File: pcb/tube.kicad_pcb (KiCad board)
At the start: 2 copper layers, 99.1 x 116.8 mm, 80 parts, among them J1 Screw_Terminal_01x02, J10 LED_[5..8], J11 LED_[1..4], J2 Screw_Terminal_01x02, J3 Screw_Terminal_01x02, J4 Conn_01x04_Pin, J5 Conn_01x08_Pin, J6 Conn_01x05_Pin, U1 INA226, U10 74LS32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

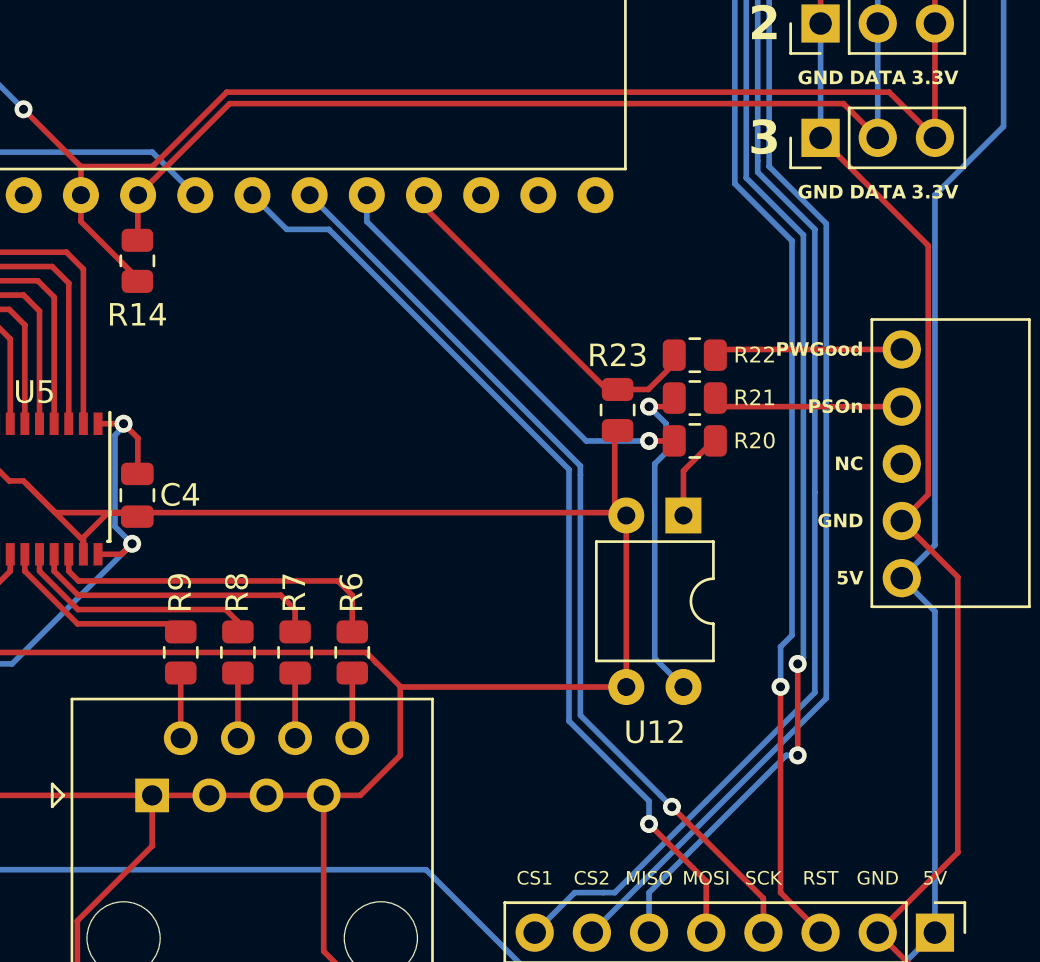
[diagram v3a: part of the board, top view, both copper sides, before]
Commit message: PCB: Add Optocoppler For PWGood
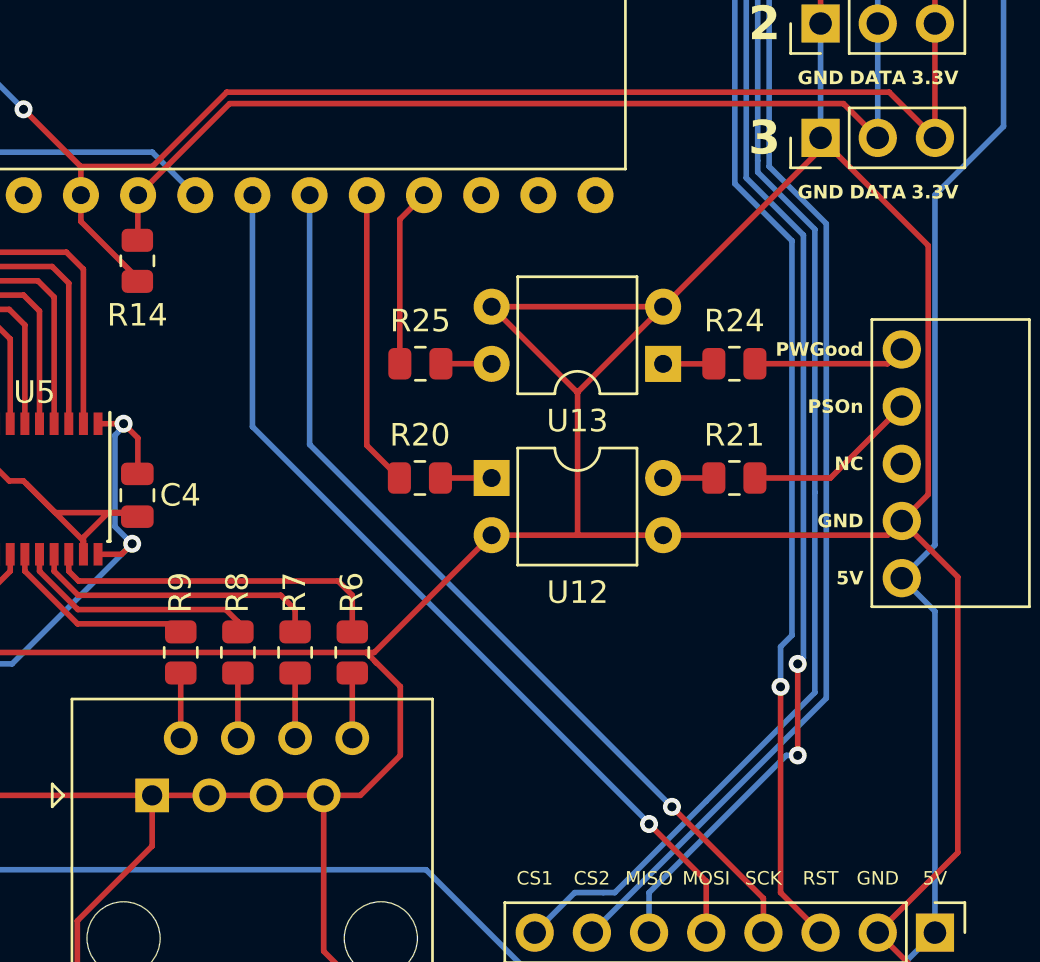
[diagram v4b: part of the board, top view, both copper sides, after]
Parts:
- removed R22: 5kΩ, Resistor_SMD:R_0805_2012Metric
- removed R23: 10kΩ, Resistor_SMD:R_0805_2012Metric
- added R24: 330Ω, Resistor_SMD:R_0805_2012Metric, F.Cu at (227.3, 184.8)
- added R25: 330Ω, Resistor_SMD:R_0805_2012Metric, F.Cu at (213.4, 184.8)
- added U13: PC817, Package_DIP:DIP-4_W7.62mm, F.Cu at (224.1, 184.8)
- moved R20 12.3 mm to (213.3, 189.9)
- moved U12 8.69 mm to (216.5, 189.9), turned to 0 degrees
- moved R21 3.96 mm to (227.3, 189.9)
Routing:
- net GND: track 1026.6 -> 1044.9 mm
- net Net-(R21-Pad2): track 14.7 -> 2.25 mm, vias 1 -> 0
- net Net-(U4-29_TX7): track 16.1 -> 8.45 mm
- net Net-(U4-28_RX7): track 19.0 -> 13.2 mm, vias 1 -> 0
- net Net-(R25-Pad2): track 0.00 -> 2.25 mm
- net Net-(R24-Pad1): track 0.00 -> 2.25 mm
- net Net-(R20-Pad1): track 3.86 -> 2.26 mm
- net /PWGood: track 8.37 -> 6.79 mm
- net /MOSI: track 42.2 -> 41.1 mm
- net /PSOn: track 8.64 -> 8.04 mm

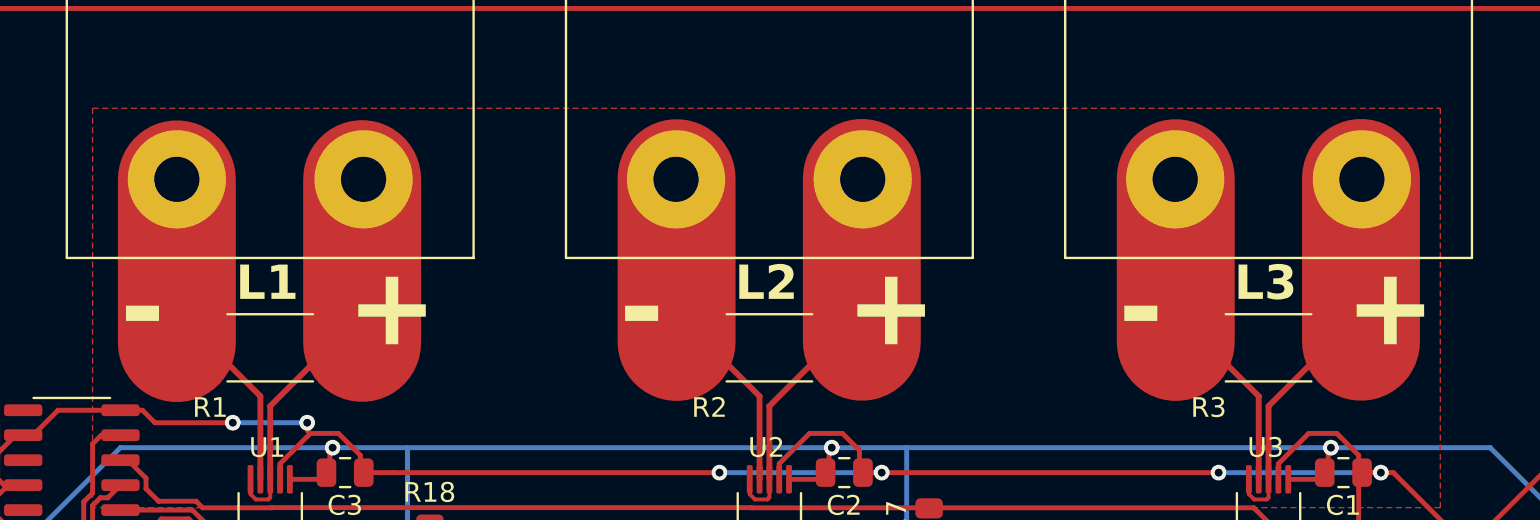
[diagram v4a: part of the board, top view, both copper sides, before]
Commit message: PCB: Tweak Shunt Trace
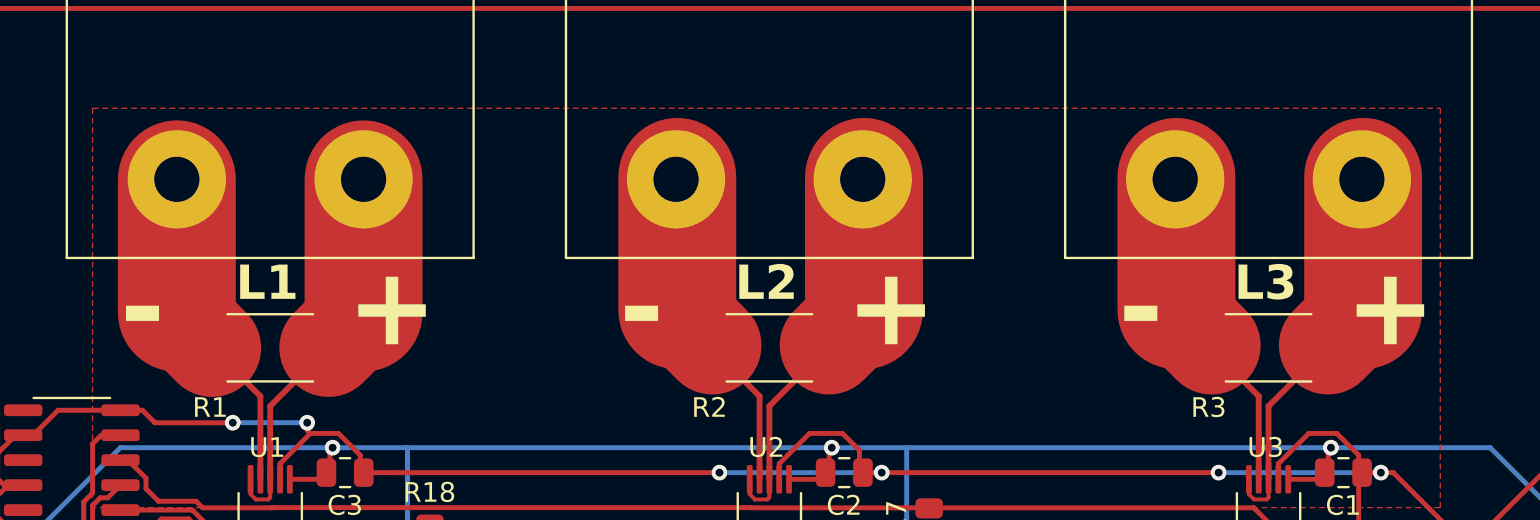
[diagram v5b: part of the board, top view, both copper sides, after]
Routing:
- net /Vin3+: track 19.1 -> 20.1 mm
- net /Vin1-: track 16.0 -> 17.0 mm
- net /Vin1+: track 19.1 -> 20.1 mm
- net /Vin3-: track 16.0 -> 17.0 mm
- net /Vin2-: track 16.0 -> 17.0 mm
- net /Vin2+: track 19.1 -> 20.1 mm
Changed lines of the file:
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@@
   (segment (start 172.235 131.57) (end 176.045 131.57) (width 0.25) (layer "B.Cu") (net 2))
   (segment (start 231.29 143) (end 230.02 144.27) (width 0.25) (layer "B.Cu") (net 2))
+  (segment (start 164.31 124.7025) (end 166.0975 126.49) (width 5) (layer "F.Cu") (net 3))
   (segment (start 168.56 133.18) (end 168.56 128.9525) (width 0.3) (layer "F.Cu") (net 3))
   (segment (start 168.56 128.9525) (end 166.0975 126.49) (width 0.3) (layer "F.Cu") (net 3))
-  (segment (start 164.31 117.915) (end 164.31 126.25) (width 6) (layer "F.Cu") (net 3))
-  (segment (start 173.736 117.903) (end 173.736 126.238) (width 6) (layer "F.Cu") (net 4))
+  (segment (start 164.31 117.915) (end 164.31 124.7025) (width 6) (layer "F.Cu") (net 3))
   (segment (start 169.06 129.4525) (end 172.0225 126.49) (width 0.3) (layer "F.Cu") (net 4))
   (segment (start 169.06 133.18) (end 169.06 129.4525) (width 0.3) (layer "F.Cu") (net 4))
   (segment (start 168.06 133.93741) (end 168.32759 134.205) (width 0.2) (layer "F.Cu") (net 4))
+  (segment (start 173.81 124.7025) (end 172.0225 126.49) (width 5) (layer "F.Cu") (net 4))
   (segment (start 168.06 133.18) (end 168.06 133.93741) (width 0.2) (layer "F.Cu") (net 4))
   (segment (start 168.32759 134.205) (end 168.965 134.205) (width 0.2) (layer "F.Cu") (net 4))
+  (segment (start 173.81 117.915) (end 173.81 124.7025) (width 6) (layer "F.Cu") (net 4))
   (segment (start 169.06 134.11) (end 169.06 133.18) (width 0.2) (layer "F.Cu") (net 4))
   (segment (start 168.965 134.205) (end 169.06 134.11) (width 0.2) (layer "F.Cu") (net 4))
+  (segment (start 189.7725 117.79) (end 189.7725 124.5775) (width 6) (layer "F.Cu") (net 5))
   (segment (start 193.96 128.9525) (end 191.4975 126.49) (width 0.3) (layer "F.Cu") (net 5))
-  (segment (start 189.738 117.856) (end 189.738 126.191) (width 6) (layer "F.Cu") (net 5))
   (segment (start 193.96 133.18) (end 193.96 128.9525) (width 0.3) (layer "F.Cu") (net 5))
+  (segment (start 189.7725 124.5775) (end 191.56 126.365) (width 5) (layer "F.Cu") (net 5))
   (segment (start 194.46 133.18) (end 194.46 129.4525) (width 0.3) (layer "F.Cu") (net 6))
-  (segment (start 199.164 117.844) (end 199.164 126.179) (width 6) (layer "F.Cu") (net 6))
+  (segment (start 199.2725 124.5775) (end 197.485 126.365) (width 5) (layer "F.Cu") (net 6))
   (segment (start 194.46 134.11) (end 194.46 133.18) (width 0.2) (layer "F.Cu") (net 6))
   (segment (start 194.365 134.205) (end 194.46 134.11) (width 0.2) (layer "F.Cu") (net 6))
   (segment (start 193.46 133.93741) (end 193.72759 134.205) (width 0.2) (layer "F.Cu") (net 6))
+  (segment (start 199.2725 117.79) (end 199.2725 124.5775) (width 6) (layer "F.Cu") (net 6))
   (segment (start 193.72759 134.205) (end 194.365 134.205) (width 0.2) (layer "F.Cu") (net 6))
   (segment (start 194.46 129.4525) (end 197.4225 126.49) (width 0.3) (layer "F.Cu") (net 6))
   (segment (start 193.46 133.18) (end 193.46 133.93741) (width 0.2) (layer "F.Cu") (net 6))
   (segment (start 219.36 128.9525) (end 216.8975 126.49) (width 0.3) (layer "F.Cu") (net 7))
-  (segment (start 215.138 117.856) (end 215.138 126.191) (width 6) (layer "F.Cu") (net 7))
+  (segment (start 215.1725 124.5775) (end 216.96 126.365) (width 5) (layer "F.Cu") (net 7))
+  (segment (start 215.1725 117.79) (end 215.1725 124.5775) (width 6) (layer "F.Cu") (net 7))
   (segment (start 219.36 133.18) (end 219.36 128.9525) (width 0.3) (layer "F.Cu") (net 7))
   (segment (start 219.86 133.18) (end 219.86 129.4525) (width 0.3) (layer "F.Cu") (net 8))
   (segment (start 219.86 134.11) (end 219.86 133.18) (width 0.2) (layer "F.Cu") (net 8))
+  (segment (start 224.6725 117.79) (end 224.6725 124.5775) (width 6) (layer "F.Cu") (net 8))
+  (segment (start 224.6725 124.5775) (end 222.885 126.365) (width 5) (layer "F.Cu") (net 8))
   (segment (start 219.86 129.4525) (end 222.8225 126.49) (width 0.3) (layer "F.Cu") (net 8))
-  (segment (start 224.564 117.844) (end 224.564 126.179) (width 6) (layer "F.Cu") (net 8))
   (segment (start 218.86 133.18) (end 218.86 133.93741) (width 0.2) (layer "F.Cu") (net 8))
   (segment (start 219.12759 134.205) (end 219.765 134.205) (width 0.2) (layer "F.Cu") (net 8))

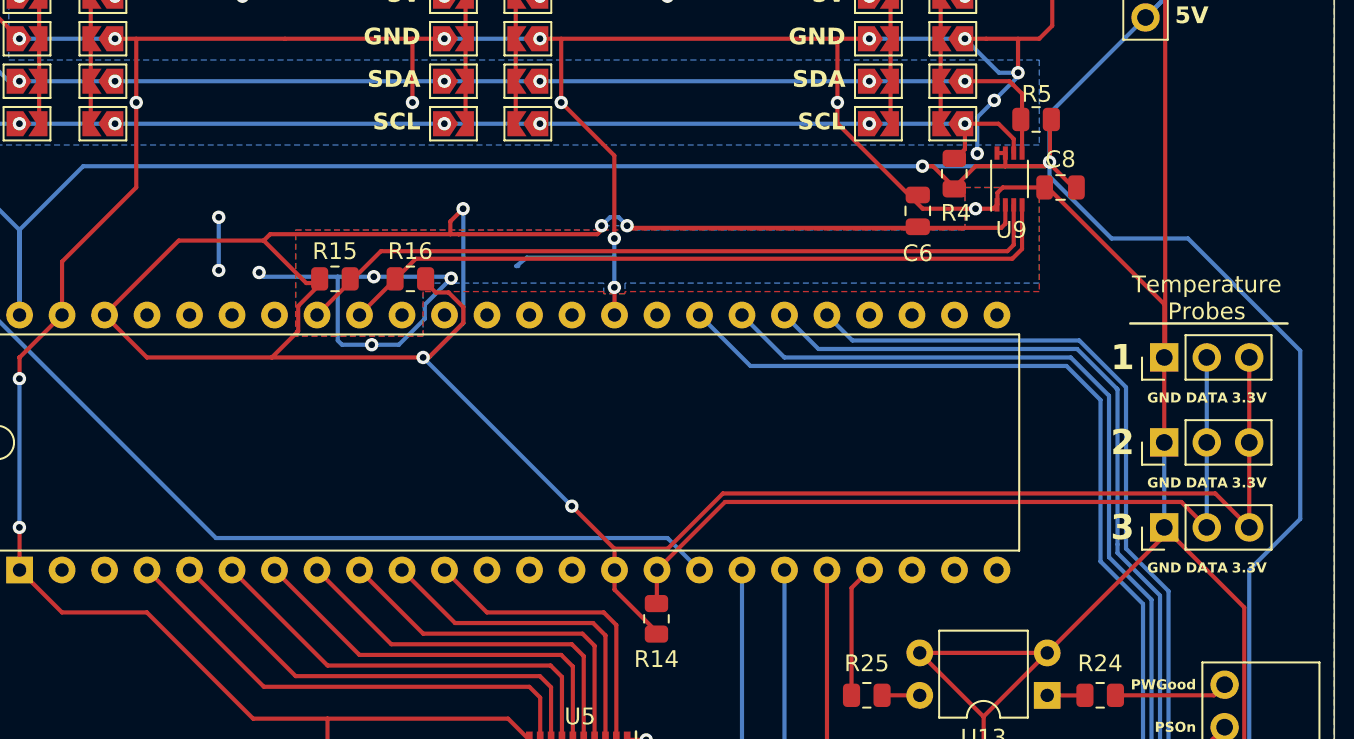
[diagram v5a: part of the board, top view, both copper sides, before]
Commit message: PCB: Improve Power Traces
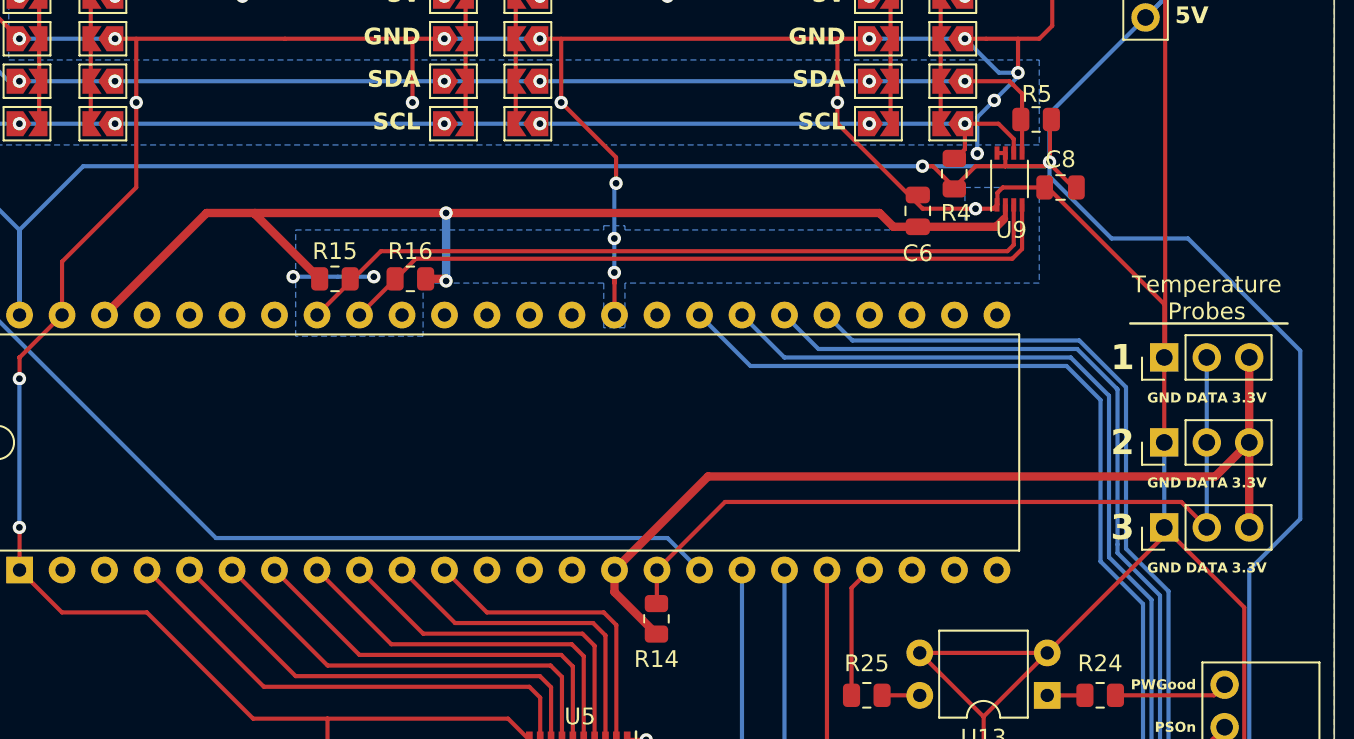
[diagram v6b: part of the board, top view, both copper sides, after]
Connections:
- R14 pad 1: +3.3V -> /+3.3V1
- U4 pad 15: +3.3V -> /+3.3V1
- U6 pad 3: +3.3V -> /+3.3V1
- U7 pad 3: +3.3V -> /+3.3V1
- U8 pad 3: +3.3V -> /+3.3V1
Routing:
- net +3.3V: track 180.2 -> 68.5 mm, vias 5 -> 2
- net /+3.3V1: track 0.00 -> 56.3 mm
- net GND: track 1044.9 -> 1016.4 mm, vias 32 -> 29

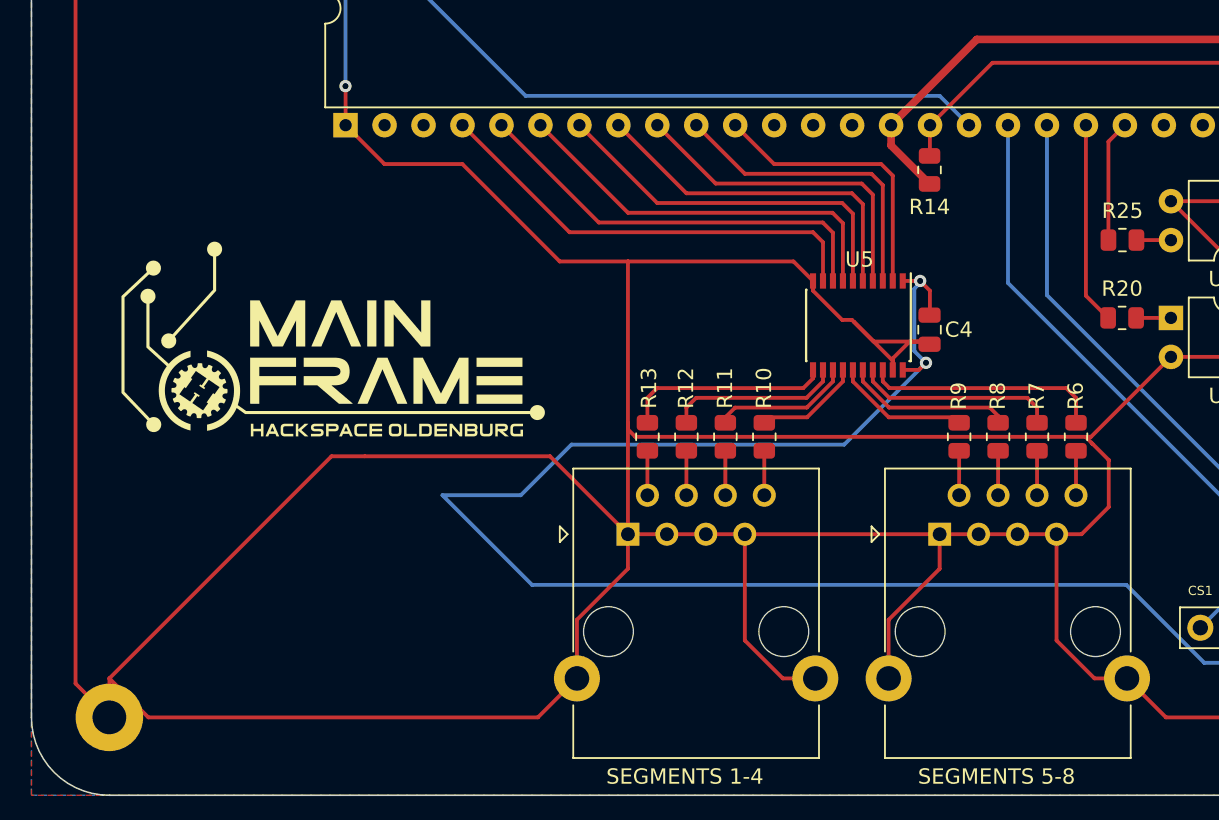
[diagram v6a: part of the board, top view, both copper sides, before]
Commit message: PCB: Add 10k PWGood Pullup
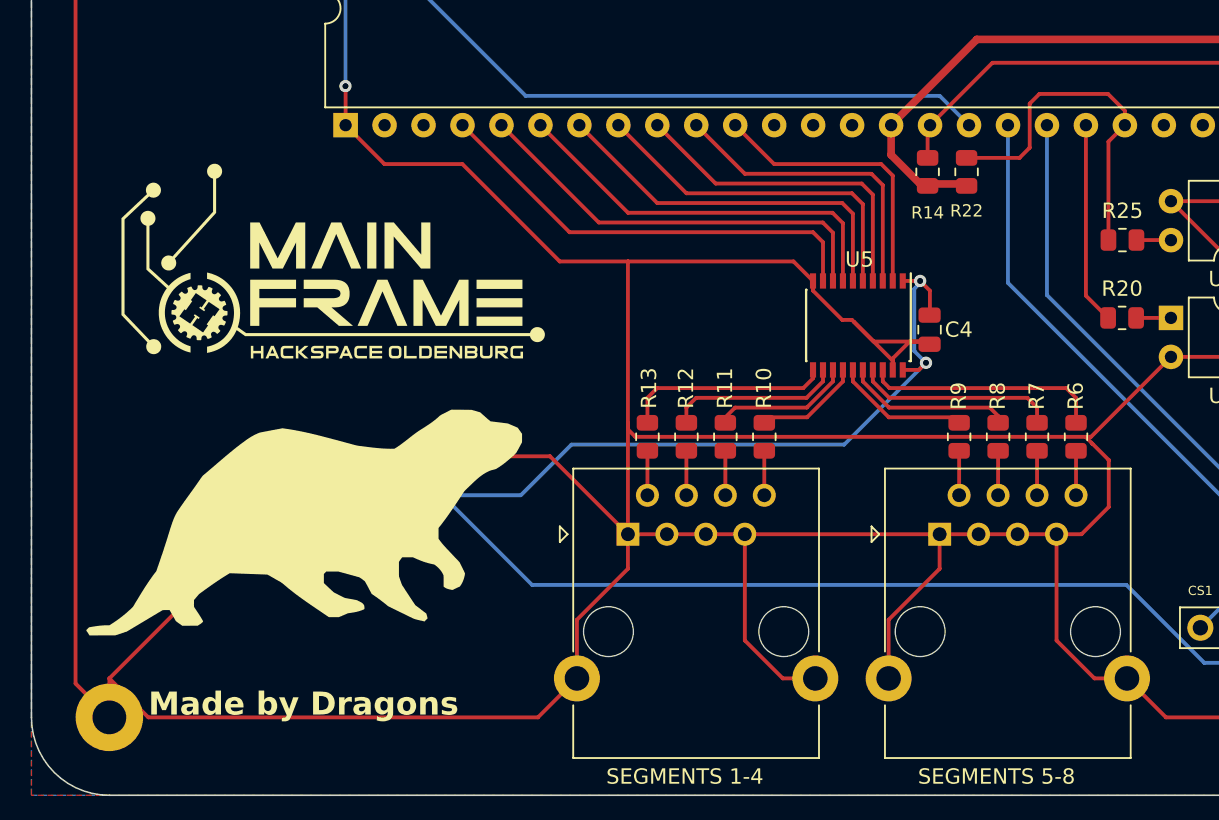
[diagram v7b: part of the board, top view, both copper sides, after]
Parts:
- added R22: 10kΩ, Resistor_SMD:R_0805_2012Metric, F.Cu at (203.2, 180.3)
- added REF**: Otter, Custom:Otter, F.Cu at (160.0, 203.2)
- moved REF** 5.08 mm to (162.6, 185.4)
- moved R14 0.18 mm to (200.7, 180.3)
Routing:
- net Net-(U4-29_TX7): track 8.45 -> 23.6 mm
- net /+3.3V1: track 56.3 -> 59.3 mm
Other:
- board text added: "Made by Dragons"
